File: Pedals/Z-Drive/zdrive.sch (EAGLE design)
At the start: 28 parts, among them IC1 MC1458P, Q1 2N7000, Q2 2N7000

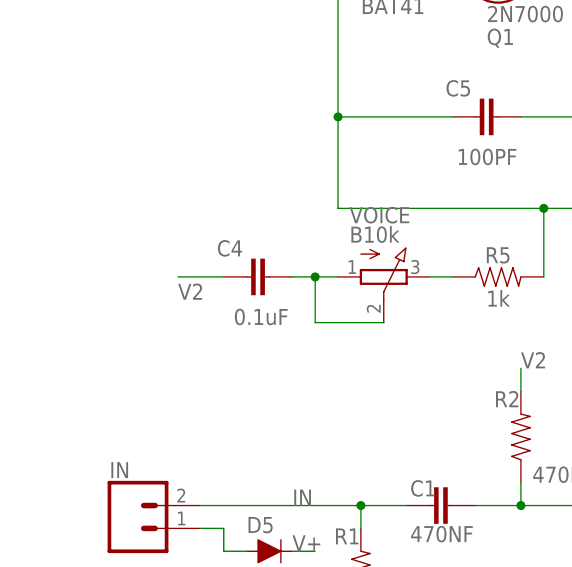
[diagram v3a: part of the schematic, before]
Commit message: Adding switch for capacitor
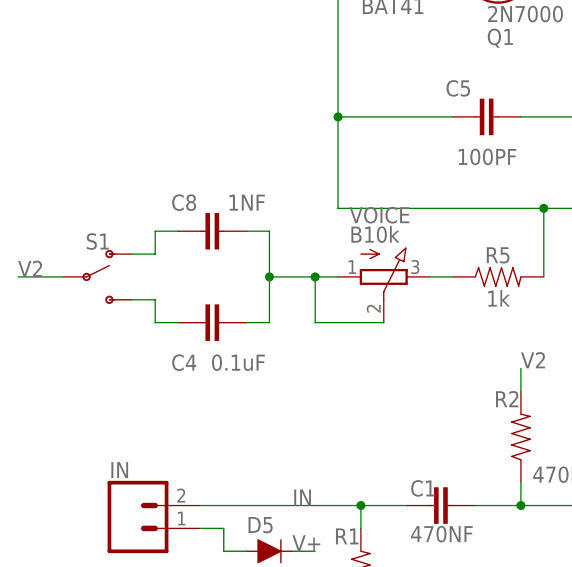
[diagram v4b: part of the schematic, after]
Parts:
- added C8: 1NF, Custom-Parts:1NF
- added S1: (no value), SparkFun-Switches:SWITCH-SPDT-PTH-11.6X4.0MM
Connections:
- new net N$11: C4.1, S1.S
- new net N$12: C8.1, S1.O
- net N$7: now also C8.2
- net V2: now also S1.P; no longer C4.1
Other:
- moved on the sheet: C4
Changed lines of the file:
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@@
 <part name="OUT" library="SparkFun-Connectors" library_urn="urn:adsk.eagle:library:513" deviceset="CONN_02" device="" package3d_urn="urn:adsk.eagle:package:38039/1"/>
 <part name="D5" library="SparkFun-DiscreteSemi" library_urn="urn:adsk.eagle:library:514" deviceset="DIODE" device="-KIT2" package3d_urn="urn:adsk.eagle:package:38455/1" value="BAT41"/>
+<part name="C8" library="Custom-Parts" deviceset="1NF" device=""/>
+<part name="S1" library="SparkFun-Switches" library_urn="urn:adsk.eagle:library:535" deviceset="SWITCH-SPDT" device="-PTH-11.6X4.0MM" package3d_urn="urn:adsk.eagle:package:40177/1"/>
 </parts>
 <sheets>
@@
 <attribute name="VALUE" x="0" y="72.136" size="1.778" layer="96" font="vector" align="top-center"/>
 </instance>
-<instance part="C4" gate="G$1" x="-25.4" y="73.66" smashed="yes" rot="R90">
-<attribute name="NAME" x="-28.321" y="77.724" size="1.778" layer="95" font="vector" rot="R180"/>
-<attribute name="VALUE" x="-23.241" y="70.104" size="1.778" layer="96" font="vector" rot="R180"/>
+<instance part="C4" gate="G$1" x="-30.48" y="68.58" smashed="yes" rot="R90">
+<attribute name="NAME" x="-33.401" y="65.024" size="1.778" layer="95" font="vector" rot="R180"/>
+<attribute name="VALUE" x="-25.781" y="65.024" size="1.778" layer="96" font="vector" rot="R180"/>
 </instance>
 <instance part="C5" gate="G$1" x="0" y="91.44" smashed="yes" rot="R90">
@@
 <attribute name="NAME" x="-27.94" y="45.212" size="1.778" layer="95" font="vector"/>
 <attribute name="VALUE" x="-27.94" y="41.148" size="1.778" layer="96" font="vector" align="top-left"/>
+</instance>
+<instance part="C8" gate="G$1" x="-30.48" y="78.74" smashed="yes" rot="R90">
+<attribute name="NAME" x="-33.401" y="82.804" size="1.778" layer="95" font="vector" rot="R180"/>
+<attribute name="VALUE" x="-25.781" y="82.804" size="1.778" layer="96" font="vector" rot="R180"/>
+</instance>
+<instance part="S1" gate="1" x="-45.72" y="73.66" smashed="yes">
+<attribute name="NAME" x="-44.45" y="76.708" size="1.778" layer="95" font="vector" align="bottom-center"/>
+<attribute name="VALUE" x="-44.704" y="70.358" size="1.778" layer="96" font="vector" align="top-center"/>
 </instance>
 </instances>
@@
 <net name="V2" class="0">
 <segment>
-<pinref part="C4" gate="G$1" pin="1"/>
-<wire x1="-30.48" y1="73.66" x2="-35.56" y2="73.66" width="0.1524" layer="91"/>
-<label x="-35.56" y="71.12" size="1.778" layer="95"/>
-</segment>
-<segment>
 <pinref part="R6" gate="G$1" pin="2"/>
 <pinref part="R7" gate="G$1" pin="1"/>
@@
 <label x="2.54" y="63.5" size="1.778" layer="95"/>
 </segment>
+<segment>
+<pinref part="S1" gate="1" pin="P"/>
+<wire x1="-48.26" y1="73.66" x2="-53.34" y2="73.66" width="0.1524" layer="91"/>
+<label x="-53.34" y="73.66" size="1.778" layer="95"/>
+</segment>
 </net>
 <net name="N$6" class="0">
@@
 <segment>
 <wire x1="-17.78" y1="73.66" x2="-20.32" y2="73.66" width="0.1524" layer="91"/>
-<wire x1="-20.32" y1="73.66" x2="-22.86" y2="73.66" width="0.1524" layer="91"/>
 <wire x1="-12.7" y1="68.58" x2="-20.32" y2="68.58" width="0.1524" layer="91"/>
 <wire x1="-20.32" y1="68.58" x2="-20.32" y2="73.66" width="0.1524" layer="91"/>
+<pinref part="VOICE" gate="G$1" pin="A"/>
+<pinref part="VOICE" gate="G$1" pin="S"/>
+<pinref part="C8" gate="G$1" pin="2"/>
+<wire x1="-27.94" y1="78.74" x2="-25.4" y2="78.74" width="0.1524" layer="91"/>
+<wire x1="-25.4" y1="78.74" x2="-25.4" y2="73.66" width="0.1524" layer="91"/>
+<wire x1="-25.4" y1="73.66" x2="-20.32" y2="73.66" width="0.1524" layer="91"/>
 <junction x="-20.32" y="73.66"/>
 <pinref part="C4" gate="G$1" pin="2"/>
-<pinref part="VOICE" gate="G$1" pin="A"/>
-<pinref part="VOICE" gate="G$1" pin="S"/>
+<wire x1="-27.94" y1="68.58" x2="-25.4" y2="68.58" width="0.1524" layer="91"/>
+<wire x1="-25.4" y1="68.58" x2="-25.4" y2="73.66" width="0.1524" layer="91"/>
+<junction x="-25.4" y="73.66"/>
 </segment>
 </net>
@@
 </segment>
 </net>
+<net name="N$11" class="0">
+<segment>
+<pinref part="S1" gate="1" pin="S"/>
+<wire x1="-40.64" y1="71.12" x2="-38.1" y2="71.12" width="0.1524" layer="91"/>
+<wire x1="-38.1" y1="71.12" x2="-38.1" y2="68.58" width="0.1524" layer="91"/>
+<pinref part="C4" gate="G$1" pin="1"/>
+<wire x1="-38.1" y1="68.58" x2="-35.56" y2="68.58" width="0.1524" layer="91"/>
+</segment>
+</net>
+<net name="N$12" class="0">
+<segment>
+<pinref part="S1" gate="1" pin="O"/>
+<wire x1="-40.64" y1="76.2" x2="-38.1" y2="76.2" width="0.1524" layer="91"/>
+<wire x1="-38.1" y1="76.2" x2="-38.1" y2="78.74" width="0.1524" layer="91"/>
+<pinref part="C8" gate="G$1" pin="1"/>
+<wire x1="-38.1" y1="78.74" x2="-35.56" y2="78.74" width="0.1524" layer="91"/>
+</segment>
+</net>

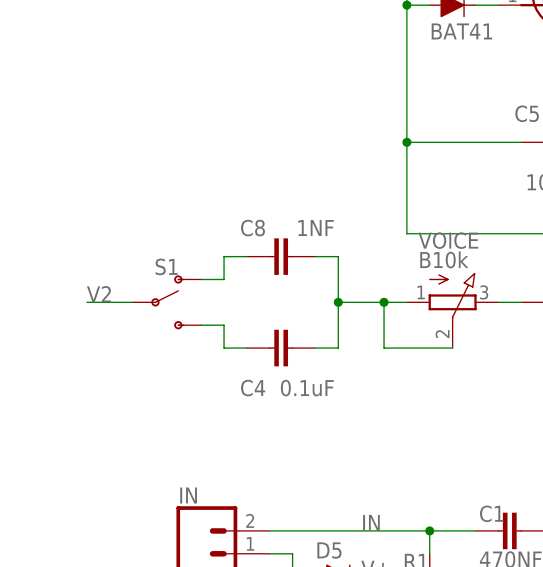
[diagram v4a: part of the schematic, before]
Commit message: Update switch to correct footprint size
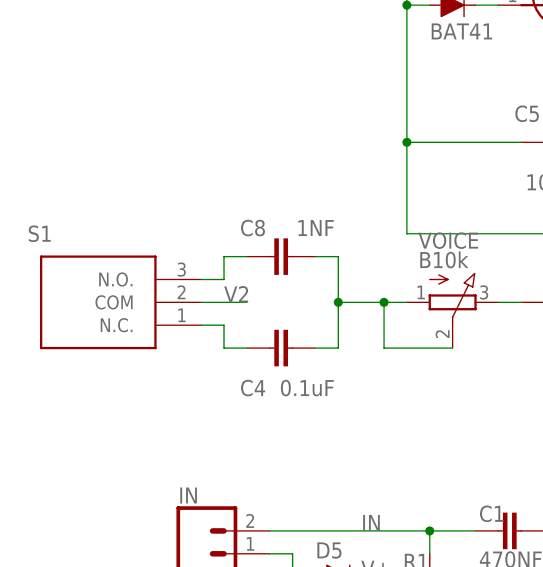
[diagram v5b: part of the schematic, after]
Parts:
- S1: value (none) -> 100SP1T1B2M2QE; device SparkFun-Switches:SWITCH-SPDT-PTH-11.6X4.0MM -> SamacSys_Parts:100SP1T1B2M2QE
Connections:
- net N$11: now also S1.N.C.; no longer S1.S
- net N$12: now also S1.N.O.; no longer S1.O
- net V2: now also S1.COM; no longer S1.P
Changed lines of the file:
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@@
 <part name="D5" library="SparkFun-DiscreteSemi" library_urn="urn:adsk.eagle:library:514" deviceset="DIODE" device="-KIT2" package3d_urn="urn:adsk.eagle:package:38455/1" value="BAT41"/>
 <part name="C8" library="Custom-Parts" deviceset="1NF" device=""/>
-<part name="S1" library="SparkFun-Switches" library_urn="urn:adsk.eagle:library:535" deviceset="SWITCH-SPDT" device="-PTH-11.6X4.0MM" package3d_urn="urn:adsk.eagle:package:40177/1"/>
+<part name="S1" library="SamacSys_Parts" deviceset="100SP1T1B2M2QE" device=""/>
 </parts>
 <sheets>
@@
 <attribute name="VALUE" x="-25.781" y="82.804" size="1.778" layer="96" font="vector" rot="R180"/>
 </instance>
-<instance part="S1" gate="1" x="-45.72" y="73.66" smashed="yes">
-<attribute name="NAME" x="-44.45" y="76.708" size="1.778" layer="95" font="vector" align="bottom-center"/>
-<attribute name="VALUE" x="-44.704" y="70.358" size="1.778" layer="96" font="vector" align="top-center"/>
+<instance part="S1" gate="G$1" x="-40.64" y="71.12" smashed="yes" rot="R180">
+<attribute name="NAME" x="-57.15" y="81.28" size="1.778" layer="95" rot="R180" align="center-left"/>
 </instance>
 </instances>
@@
 </segment>
 <segment>
-<pinref part="S1" gate="1" pin="P"/>
-<wire x1="-48.26" y1="73.66" x2="-53.34" y2="73.66" width="0.1524" layer="91"/>
-<label x="-53.34" y="73.66" size="1.778" layer="95"/>
+<wire x1="-35.56" y1="73.66" x2="-40.64" y2="73.66" width="0.1524" layer="91"/>
+<label x="-38.1" y="73.66" size="1.778" layer="95"/>
+<pinref part="S1" gate="G$1" pin="COM"/>
 </segment>
 </net>
@@
 <net name="N$11" class="0">
 <segment>
-<pinref part="S1" gate="1" pin="S"/>
 <wire x1="-40.64" y1="71.12" x2="-38.1" y2="71.12" width="0.1524" layer="91"/>
 <wire x1="-38.1" y1="71.12" x2="-38.1" y2="68.58" width="0.1524" layer="91"/>
 <pinref part="C4" gate="G$1" pin="1"/>
 <wire x1="-38.1" y1="68.58" x2="-35.56" y2="68.58" width="0.1524" layer="91"/>
+<pinref part="S1" gate="G$1" pin="N.C."/>
 </segment>
 </net>
 <net name="N$12" class="0">
 <segment>
-<pinref part="S1" gate="1" pin="O"/>
 <wire x1="-40.64" y1="76.2" x2="-38.1" y2="76.2" width="0.1524" layer="91"/>
 <wire x1="-38.1" y1="76.2" x2="-38.1" y2="78.74" width="0.1524" layer="91"/>
 <pinref part="C8" gate="G$1" pin="1"/>
 <wire x1="-38.1" y1="78.74" x2="-35.56" y2="78.74" width="0.1524" layer="91"/>
-</segment>
-</net>
+<pinref part="S1" gate="G$1" pin="N.O."/>
+</segment>
+</net>

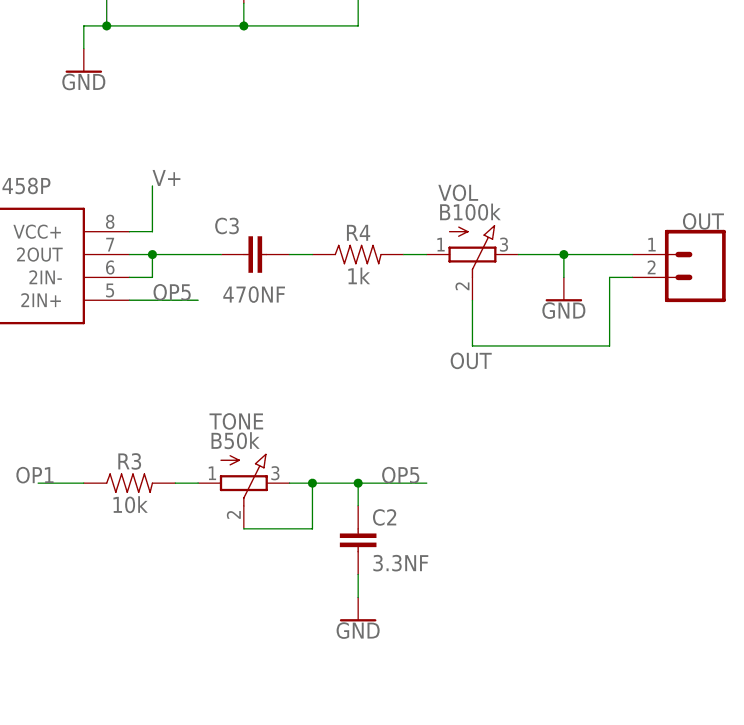
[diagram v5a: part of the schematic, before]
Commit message: Flipped the volume and tone pots
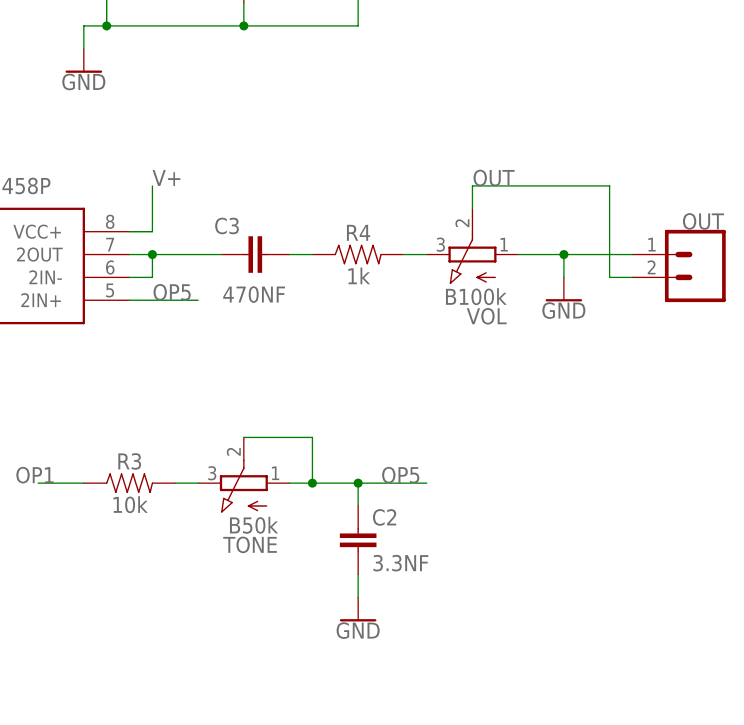
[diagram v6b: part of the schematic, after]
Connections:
- net GND: now also VOL.A; no longer VOL.E
- net N$1: now also TONE.E; no longer TONE.A
- net N$4: now also VOL.E; no longer VOL.A
- net OP5: now also TONE.A; no longer TONE.E
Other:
- moved on the sheet: TONE, VOL
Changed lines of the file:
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@@
 <attribute name="VALUE" x="-16.51" y="77.47" size="1.778" layer="96"/>
 </instance>
-<instance part="TONE" gate="G$1" x="60.96" y="55.88" smashed="yes" rot="R270">
-<attribute name="NAME" x="57.15" y="61.849" size="1.778" layer="95"/>
-<attribute name="VALUE" x="57.15" y="59.69" size="1.778" layer="96"/>
-</instance>
-<instance part="VOL" gate="G$1" x="86.36" y="81.28" smashed="yes" rot="R270">
-<attribute name="NAME" x="82.55" y="87.249" size="1.778" layer="95"/>
-<attribute name="VALUE" x="82.55" y="85.09" size="1.778" layer="96"/>
+<instance part="TONE" gate="G$1" x="60.96" y="55.88" smashed="yes" rot="R90">
+<attribute name="NAME" x="64.77" y="49.911" size="1.778" layer="95" rot="R180"/>
+<attribute name="VALUE" x="64.77" y="52.07" size="1.778" layer="96" rot="R180"/>
+</instance>
+<instance part="VOL" gate="G$1" x="86.36" y="81.28" smashed="yes" rot="R90">
+<attribute name="NAME" x="90.17" y="75.311" size="1.778" layer="95" rot="R180"/>
+<attribute name="VALUE" x="90.17" y="77.47" size="1.778" layer="96" rot="R180"/>
 </instance>
 <instance part="IN" gate="G$1" x="-40.64" y="45.72" smashed="yes">
@@
 </segment>
 <segment>
-<wire x1="91.44" y1="81.28" x2="96.52" y2="81.28" width="0.1524" layer="91"/>
 <pinref part="GND4" gate="1" pin="GND"/>
 <wire x1="96.52" y1="81.28" x2="96.52" y2="78.74" width="0.1524" layer="91"/>
-<pinref part="VOL" gate="G$1" pin="E"/>
 <pinref part="OUT" gate="G$1" pin="1"/>
 <wire x1="96.52" y1="81.28" x2="104.14" y2="81.28" width="0.1524" layer="91"/>
+<pinref part="VOL" gate="G$1" pin="A"/>
+<wire x1="91.44" y1="81.28" x2="96.52" y2="81.28" width="0.1524" layer="91"/>
 <junction x="96.52" y="81.28"/>
 </segment>
@@
 </segment>
 </net>
-<net name="N$1" class="0">
-<segment>
-<pinref part="R3" gate="G$1" pin="2"/>
-<wire x1="53.34" y1="55.88" x2="55.88" y2="55.88" width="0.1524" layer="91"/>
-<pinref part="TONE" gate="G$1" pin="A"/>
-</segment>
-</net>
 <net name="OP5" class="0">
 <segment>
-<wire x1="66.04" y1="55.88" x2="68.58" y2="55.88" width="0.1524" layer="91"/>
-<wire x1="68.58" y1="55.88" x2="73.66" y2="55.88" width="0.1524" layer="91"/>
 <wire x1="73.66" y1="55.88" x2="81.28" y2="55.88" width="0.1524" layer="91"/>
-<wire x1="60.96" y1="50.8" x2="68.58" y2="50.8" width="0.1524" layer="91"/>
-<wire x1="68.58" y1="50.8" x2="68.58" y2="55.88" width="0.1524" layer="91"/>
-<junction x="68.58" y="55.88"/>
 <wire x1="73.66" y1="55.88" x2="73.66" y2="53.34" width="0.1524" layer="91"/>
-<junction x="73.66" y="55.88"/>
 <pinref part="C2" gate="G$1" pin="1"/>
 <label x="76.2" y="55.88" size="1.778" layer="95"/>
-<pinref part="TONE" gate="G$1" pin="E"/>
+<pinref part="TONE" gate="G$1" pin="A"/>
+<wire x1="66.04" y1="55.88" x2="68.58" y2="55.88" width="0.1524" layer="91"/>
+<junction x="73.66" y="55.88"/>
 <pinref part="TONE" gate="G$1" pin="S"/>
+<wire x1="68.58" y1="55.88" x2="73.66" y2="55.88" width="0.1524" layer="91"/>
+<wire x1="60.96" y1="60.96" x2="68.58" y2="60.96" width="0.1524" layer="91"/>
+<wire x1="68.58" y1="60.96" x2="68.58" y2="55.88" width="0.1524" layer="91"/>
+<junction x="68.58" y="55.88"/>
 </segment>
 <segment>
@@
 <wire x1="66.04" y1="81.28" x2="68.58" y2="81.28" width="0.1524" layer="91"/>
 <pinref part="R4" gate="G$1" pin="1"/>
-</segment>
-</net>
-<net name="N$4" class="0">
-<segment>
-<pinref part="R4" gate="G$1" pin="2"/>
-<wire x1="78.74" y1="81.28" x2="81.28" y2="81.28" width="0.1524" layer="91"/>
-<pinref part="VOL" gate="G$1" pin="A"/>
 </segment>
 </net>
@@
 <net name="OUT" class="0">
 <segment>
-<wire x1="86.36" y1="76.2" x2="86.36" y2="71.12" width="0.1524" layer="91"/>
-<label x="83.82" y="68.58" size="1.778" layer="95"/>
 <pinref part="VOL" gate="G$1" pin="S"/>
-<wire x1="86.36" y1="71.12" x2="101.6" y2="71.12" width="0.1524" layer="91"/>
-<wire x1="101.6" y1="71.12" x2="101.6" y2="78.74" width="0.1524" layer="91"/>
+<wire x1="86.36" y1="86.36" x2="86.36" y2="88.9" width="0.1524" layer="91"/>
+<wire x1="86.36" y1="88.9" x2="101.6" y2="88.9" width="0.1524" layer="91"/>
 <pinref part="OUT" gate="G$1" pin="2"/>
 <wire x1="101.6" y1="78.74" x2="104.14" y2="78.74" width="0.1524" layer="91"/>
+<label x="86.36" y="88.9" size="1.778" layer="95"/>
+<wire x1="101.6" y1="78.74" x2="101.6" y2="88.9" width="0.1524" layer="91"/>
 </segment>
 </net>
@@
 </segment>
 </net>
+<net name="N$4" class="0">
+<segment>
+<pinref part="R4" gate="G$1" pin="2"/>
+<pinref part="VOL" gate="G$1" pin="E"/>
+<wire x1="78.74" y1="81.28" x2="81.28" y2="81.28" width="0.1524" layer="91"/>
+</segment>
+</net>
+<net name="N$1" class="0">
+<segment>
+<pinref part="R3" gate="G$1" pin="2"/>
+<pinref part="TONE" gate="G$1" pin="E"/>
+<wire x1="53.34" y1="55.88" x2="55.88" y2="55.88" width="0.1524" layer="91"/>
+</segment>
+</net>
